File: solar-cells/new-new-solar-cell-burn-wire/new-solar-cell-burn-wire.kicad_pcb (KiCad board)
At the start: 2 copper layers, 80 x 103.5 mm, 22 parts, among them J1 Solar Cell, J2 Burn Wire

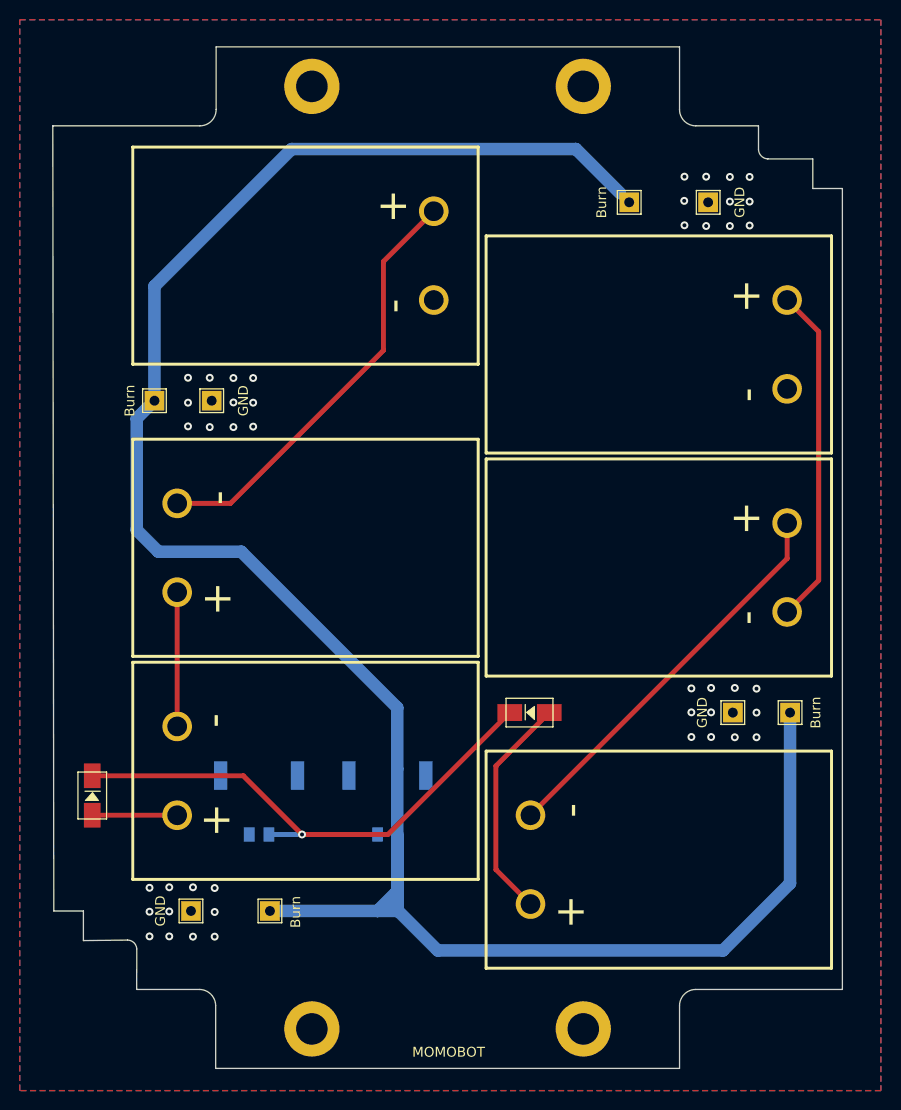
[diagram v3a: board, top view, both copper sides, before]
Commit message: fixed tracks to reduce EMI
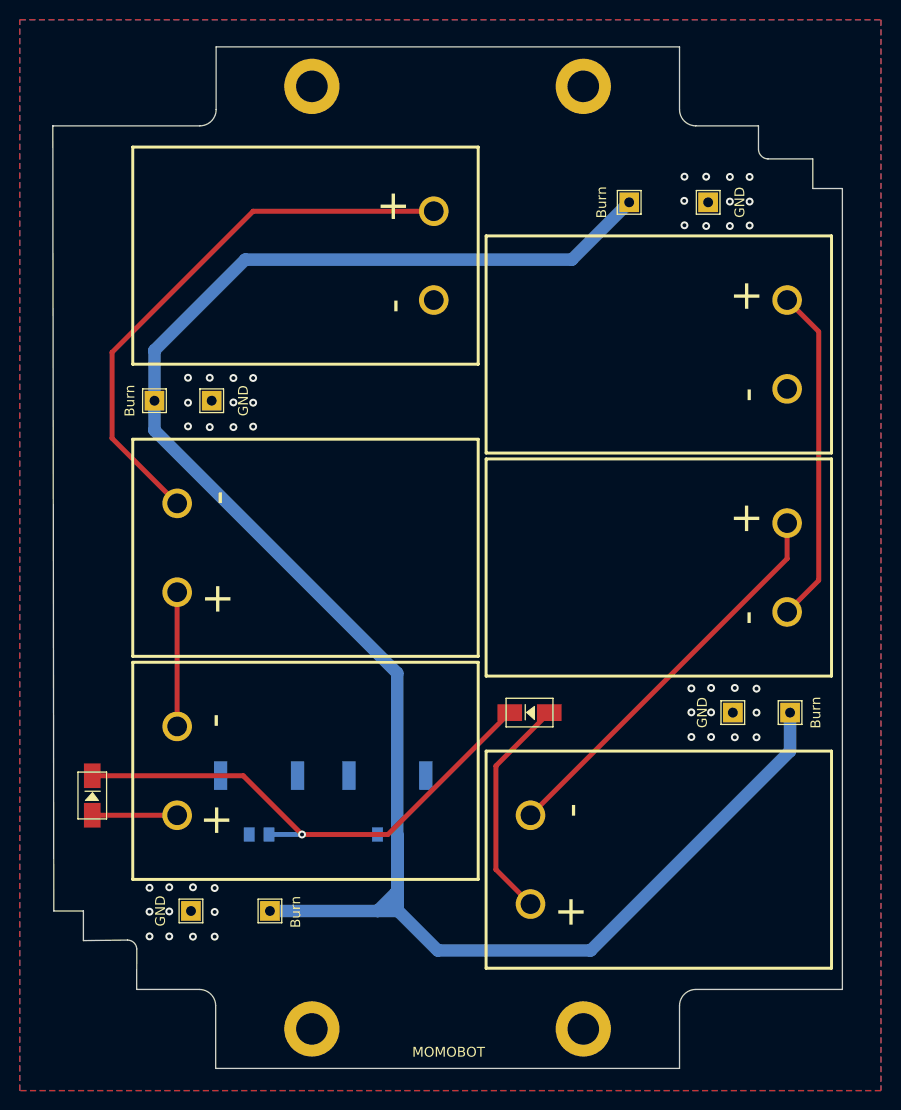
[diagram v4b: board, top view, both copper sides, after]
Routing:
- net BURN: track 220.9 -> 198.4 mm
- net Net-(SC2-Pad2): track 43.5 -> 56.6 mm
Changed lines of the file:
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@@
   (via (at 136.075 54.35) (size 0.8) (drill 0.4) (layers "F.Cu" "B.Cu") (free) (net 1))
   (segment (start 107.000001 118.725) (end 107.000001 126.3) (width 1.27) (layer "B.Cu") (net 2))
-  (segment (start 107.000001 105.700001) (end 107.000001 111.900001) (width 1.27) (layer "B.Cu") (net 2))
-  (segment (start 82.8 89.9) (end 91.2 89.9) (width 1.27) (layer "B.Cu") (net 2))
-  (segment (start 96.3 49.1) (end 82.4 63) (width 1.27) (layer "B.Cu") (net 2))
   (segment (start 105 126.3) (end 94.1 126.3) (width 1.27) (layer "B.Cu") (net 2))
-  (segment (start 82.4 63) (end 82.4 74.6) (width 1.27) (layer "B.Cu") (net 2))
+  (segment (start 111.1 130.3) (end 126.6 130.3) (width 1.27) (layer "B.Cu") (net 2))
   (segment (start 107.000001 118.55) (end 107.000001 124.399999) (width 1.27) (layer "B.Cu") (net 2))
-  (segment (start 80.6 76.4) (end 80.6 87.7) (width 1.27) (layer "B.Cu") (net 2))
+  (segment (start 146.8 110.1) (end 146.8 106.2) (width 1.27) (layer "B.Cu") (net 2))
   (segment (start 107.000001 118.55) (end 107.000001 118.725) (width 0.25) (layer "B.Cu") (net 2))
+  (segment (start 107.000001 126.3) (end 105 126.3) (width 1.27) (layer "B.Cu") (net 2))
   (segment (start 107.000001 126.200001) (end 111.1 130.3) (width 1.27) (layer "B.Cu") (net 2))
-  (segment (start 107.000001 126.3) (end 105 126.3) (width 1.27) (layer "B.Cu") (net 2))
-  (segment (start 146.8 123.5) (end 146.8 106.2) (width 1.27) (layer "B.Cu") (net 2))
-  (segment (start 111.1 130.3) (end 140 130.3) (width 1.27) (layer "B.Cu") (net 2))
-  (segment (start 80.6 87.7) (end 82.8 89.9) (width 1.27) (layer "B.Cu") (net 2))
-  (segment (start 91.2 89.9) (end 107.000001 105.700001) (width 1.27) (layer "B.Cu") (net 2))
-  (segment (start 125.1 49.1) (end 96.3 49.1) (width 1.27) (layer "B.Cu") (net 2))
-  (segment (start 129.575 53.575) (end 125.1 49.1) (width 1.27) (layer "B.Cu") (net 2))
+  (segment (start 130.5 54.5) (end 124.7 60.3) (width 1.27) (layer "B.Cu") (net 2))
+  (segment (start 107.000001 102.200001) (end 107.000001 118.55) (width 1.27) (layer "B.Cu") (net 2))
+  (segment (start 126.6 130.3) (end 146.8 110.1) (width 1.27) (layer "B.Cu") (net 2))
+  (segment (start 82.4 69.5) (end 82.4 74.6) (width 1.27) (layer "B.Cu") (net 2))
   (segment (start 106.900001 124.399999) (end 107.000001 124.399999) (width 1.27) (layer "B.Cu") (net 2))
-  (segment (start 130.5 54.5) (end 129.575 53.575) (width 0.25) (layer "B.Cu") (net 2))
+  (segment (start 82.4 77.6) (end 107.000001 102.200001) (width 1.27) (layer "B.Cu") (net 2))
+  (segment (start 124.7 60.3) (end 91.6 60.3) (width 1.27) (layer "B.Cu") (net 2))
+  (segment (start 107.000001 124.399999) (end 107.000001 126.200001) (width 1.27) (layer "B.Cu") (net 2))
   (segment (start 105 126.3) (end 106.900001 124.399999) (width 1.27) (layer "B.Cu") (net 2))
-  (segment (start 82.4 74.6) (end 80.6 76.4) (width 1.27) (layer "B.Cu") (net 2))
-  (segment (start 107.000001 124.399999) (end 107.000001 126.200001) (width 1.27) (layer "B.Cu") (net 2))
-  (segment (start 140 130.3) (end 146.8 123.5) (width 1.27) (layer "B.Cu") (net 2))
-  (segment (start 107.000001 111.900001) (end 107.000001 118.55) (width 1.27) (layer "B.Cu") (net 2))
+  (segment (start 91.6 60.3) (end 82.4 69.5) (width 1.27) (layer "B.Cu") (net 2))
+  (segment (start 82.4 74.6) (end 82.4 77.6) (width 1.27) (layer "B.Cu") (net 2))
   (segment (start 84.7 94) (end 84.7 107.6) (width 0.5) (layer "F.Cu") (net 3))
   (segment (start 84.7 116.6) (end 76.1 116.6) (width 0.5) (layer "F.Cu") (net 4))
@@
   (segment (start 117 111.6) (end 117 122.1) (width 0.5) (layer "F.Cu") (net 5))
   (segment (start 122.4 106.2) (end 117 111.6) (width 0.5) (layer "F.Cu") (net 5))
-  (segment (start 90.1 85) (end 84.7 85) (width 0.5) (layer "F.Cu") (net 6))
-  (segment (start 105.6 69.5) (end 90.1 85) (width 0.5) (layer "F.Cu") (net 6))
-  (segment (start 105.6 60.5) (end 105.6 69.5) (width 0.5) (layer "F.Cu") (net 6))
-  (segment (start 110.7 55.4) (end 105.6 60.5) (width 0.5) (layer "F.Cu") (net 6))
+  (segment (start 92.4 55.4) (end 110.7 55.4) (width 0.5) (layer "F.Cu") (net 6))
+  (segment (start 78.1 78.4) (end 78.1 69.7) (width 0.5) (layer "F.Cu") (net 6))
+  (segment (start 84.7 85) (end 78.1 78.4) (width 0.5) (layer "F.Cu") (net 6))
+  (segment (start 78.1 69.7) (end 92.4 55.4) (width 0.5) (layer "F.Cu") (net 6))
   (segment (start 146.5 90.6) (end 120.5 116.6) (width 0.5) (layer "F.Cu") (net 7))
   (segment (start 146.5 87) (end 146.5 90.6) (width 0.5) (layer "F.Cu") (net 7))
@@
   (segment (start 149.7 92.8) (end 146.5 96) (width 0.5) (layer "F.Cu") (net 8))
   (segment (start 97.35 118.55) (end 91.4 112.6) (width 0.5) (layer "F.Cu") (net 9))
-  (segment (start 97.25 118.55) (end 97.35 118.55) (width 0.25) (layer "F.Cu") (net 9))
   (segment (start 97.35 118.55) (end 106.05 118.55) (width 0.5) (layer "F.Cu") (net 9))
   (segment (start 106.05 118.55) (end 118.4 106.2) (width 0.5) (layer "F.Cu") (net 9))

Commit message: fixed routing, added vias
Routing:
- net VSOLAR: track 53.2 -> 60.9 mm
- net GND: vias 44 -> 56
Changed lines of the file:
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@@
   )
   (via (at 81.9 128.875) (size 0.8) (drill 0.4) (layers "F.Cu" "B.Cu") (free) (net 1))
-  (via (at 85.8 77.2) (size 0.8) (drill 0.4) (layers "F.Cu" "B.Cu") (free) (net 1))
+  (via (at 114.4 66.1) (size 0.8) (drill 0.4) (layers "F.Cu" "B.Cu") (free) (net 1))
+  (via (at 113.5 64.2) (size 0.8) (drill 0.4) (layers "F.Cu" "B.Cu") (free) (net 1))
   (via (at 136.8 106.175) (size 0.8) (drill 0.4) (layers "F.Cu" "B.Cu") (free) (net 1))
-  (via (at 136.1 51.9) (size 0.8) (drill 0.4) (layers "F.Cu" "B.Cu") (free) (net 1))
   (via (at 81.9 123.95) (size 0.8) (drill 0.4) (layers "F.Cu" "B.Cu") (free) (net 1))
   (via (at 140.7 51.925) (size 0.8) (drill 0.4) (layers "F.Cu" "B.Cu") (free) (net 1))
   (via (at 138.8 106.175) (size 0.8) (drill 0.4) (layers "F.Cu" "B.Cu") (free) (net 1))
-  (via (at 143.4 103.775) (size 0.8) (drill 0.4) (layers "F.Cu" "B.Cu") (free) (net 1))
+  (via (at 145.4 76.8) (size 0.8) (drill 0.4) (layers "F.Cu" "B.Cu") (free) (net 1))
   (via (at 90.4 72.3) (size 0.8) (drill 0.4) (layers "F.Cu" "B.Cu") (free) (net 1))
   (via (at 141.2 108.7) (size 0.8) (drill 0.4) (layers "F.Cu" "B.Cu") (free) (net 1))
   (via (at 90.4 74.775) (size 0.8) (drill 0.4) (layers "F.Cu" "B.Cu") (free) (net 1))
-  (via (at 85.8 72.275) (size 0.8) (drill 0.4) (layers "F.Cu" "B.Cu") (free) (net 1))
+  (via (at 144.2 70) (size 0.8) (drill 0.4) (layers "F.Cu" "B.Cu") (free) (net 1))
+  (via (at 108 66) (size 0.8) (drill 0.4) (layers "F.Cu" "B.Cu") (free) (net 1))
   (via (at 83.9 123.9) (size 0.8) (drill 0.4) (layers "F.Cu" "B.Cu") (free) (net 1))
+  (via (at 144.2 76.3) (size 0.8) (drill 0.4) (layers "F.Cu" "B.Cu") (free) (net 1))
+  (via (at 110.8 67.4) (size 0.8) (drill 0.4) (layers "F.Cu" "B.Cu") (free) (net 1))
+  (via (at 144.2 71.3) (size 0.8) (drill 0.4) (layers "F.Cu" "B.Cu") (free) (net 1))
+  (via (at 143.4 75.2) (size 0.8) (drill 0.4) (layers "F.Cu" "B.Cu") (free) (net 1))
   (via (at 83.9 126.35) (size 0.8) (drill 0.4) (layers "F.Cu" "B.Cu") (free) (net 1))
   (via (at 83.9 128.875) (size 0.8) (drill 0.4) (layers "F.Cu" "B.Cu") (free) (net 1))
   (via (at 92.4 77.225) (size 0.8) (drill 0.4) (layers "F.Cu" "B.Cu") (free) (net 1))
+  (via (at 107.3 67.2) (size 0.8) (drill 0.4) (layers "F.Cu" "B.Cu") (free) (net 1))
   (via (at 142.7 51.925) (size 0.8) (drill 0.4) (layers "F.Cu" "B.Cu") (free) (net 1))
-  (via (at 88.5 123.975) (size 0.8) (drill 0.4) (layers "F.Cu" "B.Cu") (free) (net 1))
+  (via (at 143.9 74.1) (size 0.8) (drill 0.4) (layers "F.Cu" "B.Cu") (free) (net 1))
   (via (at 136.8 108.675) (size 0.8) (drill 0.4) (layers "F.Cu" "B.Cu") (free) (net 1))
-  (via (at 88.5 128.9) (size 0.8) (drill 0.4) (layers "F.Cu" "B.Cu") (free) (net 1))
+  (via (at 144.7 75.4) (size 0.8) (drill 0.4) (layers "F.Cu" "B.Cu") (free) (net 1))
+  (via (at 108.7 68.5) (size 0.8) (drill 0.4) (layers "F.Cu" "B.Cu") (free) (net 1))
   (via (at 88 77.275) (size 0.8) (drill 0.4) (layers "F.Cu" "B.Cu") (free) (net 1))
+  (via (at 107.7 64.4) (size 0.8) (drill 0.4) (layers "F.Cu" "B.Cu") (free) (net 1))
+  (via (at 113.4 67.7) (size 0.8) (drill 0.4) (layers "F.Cu" "B.Cu") (free) (net 1))
   (via (at 92.4 72.3) (size 0.8) (drill 0.4) (layers "F.Cu" "B.Cu") (free) (net 1))
   (via (at 142.7 56.85) (size 0.8) (drill 0.4) (layers "F.Cu" "B.Cu") (free) (net 1))
-  (via (at 143.4 108.7) (size 0.8) (drill 0.4) (layers "F.Cu" "B.Cu") (free) (net 1))
+  (via (at 109.1 67.2) (size 0.8) (drill 0.4) (layers "F.Cu" "B.Cu") (free) (net 1))
   (via (at 138.8 108.675) (size 0.8) (drill 0.4) (layers "F.Cu" "B.Cu") (free) (net 1))
   (via (at 92.4 74.8) (size 0.8) (drill 0.4) (layers "F.Cu" "B.Cu") (free) (net 1))
-  (via (at 143.4 106.2) (size 0.8) (drill 0.4) (layers "F.Cu" "B.Cu") (free) (net 1))
+  (via (at 143.9 72.5) (size 0.8) (drill 0.4) (layers "F.Cu" "B.Cu") (free) (net 1))
   (via (at 138.3 56.9) (size 0.8) (drill 0.4) (layers "F.Cu" "B.Cu") (free) (net 1))
+  (via (at 143.1 70.9) (size 0.8) (drill 0.4) (layers "F.Cu" "B.Cu") (free) (net 1))
   (via (at 90.4 77.275) (size 0.8) (drill 0.4) (layers "F.Cu" "B.Cu") (free) (net 1))
-  (via (at 85.8 74.8) (size 0.8) (drill 0.4) (layers "F.Cu" "B.Cu") (free) (net 1))
+  (via (at 113.3 65.6) (size 0.8) (drill 0.4) (layers "F.Cu" "B.Cu") (free) (net 1))
   (via (at 138.3 51.9) (size 0.8) (drill 0.4) (layers "F.Cu" "B.Cu") (free) (net 1))
   (via (at 140.7 56.9) (size 0.8) (drill 0.4) (layers "F.Cu" "B.Cu") (free) (net 1))
-  (via (at 136.8 103.75) (size 0.8) (drill 0.4) (layers "F.Cu" "B.Cu") (free) (net 1))
+  (via (at 145.3 70.7) (size 0.8) (drill 0.4) (layers "F.Cu" "B.Cu") (free) (net 1))
+  (via (at 142.8 72) (size 0.8) (drill 0.4) (layers "F.Cu" "B.Cu") (free) (net 1))
   (via (at 138.8 103.7) (size 0.8) (drill 0.4) (layers "F.Cu" "B.Cu") (free) (net 1))
   (via (at 81.9 126.375) (size 0.8) (drill 0.4) (layers "F.Cu" "B.Cu") (free) (net 1))
@@
   (via (at 88 72.275) (size 0.8) (drill 0.4) (layers "F.Cu" "B.Cu") (free) (net 1))
   (via (at 140.7 54.425) (size 0.8) (drill 0.4) (layers "F.Cu" "B.Cu") (free) (net 1))
-  (via (at 136.1 56.825) (size 0.8) (drill 0.4) (layers "F.Cu" "B.Cu") (free) (net 1))
-  (via (at 88.5 126.4) (size 0.8) (drill 0.4) (layers "F.Cu" "B.Cu") (free) (net 1))
-  (via (at 136.075 54.35) (size 0.8) (drill 0.4) (layers "F.Cu" "B.Cu") (free) (net 1))
+  (via (at 110.5 68.8) (size 0.8) (drill 0.4) (layers "F.Cu" "B.Cu") (free) (net 1))
+  (via (at 112 68.5) (size 0.8) (drill 0.4) (layers "F.Cu" "B.Cu") (free) (net 1))
+  (via (at 112.4 66.8) (size 0.8) (drill 0.4) (layers "F.Cu" "B.Cu") (free) (net 1))
+  (via (at 146.1 75.9) (size 0.8) (drill 0.4) (layers "F.Cu" "B.Cu") (free) (net 1))
   (segment (start 107.000001 118.725) (end 107.000001 126.3) (width 1.27) (layer "B.Cu") (net 2))
   (segment (start 105 126.3) (end 94.1 126.3) (width 1.27) (layer "B.Cu") (net 2))
@@
   (segment (start 146.8 110.1) (end 146.8 106.2) (width 1.27) (layer "B.Cu") (net 2))
   (segment (start 107.000001 118.55) (end 107.000001 118.725) (width 0.25) (layer "B.Cu") (net 2))
+  (segment (start 125.4 59.6) (end 92.3 59.6) (width 1.27) (layer "B.Cu") (net 2))
   (segment (start 107.000001 126.3) (end 105 126.3) (width 1.27) (layer "B.Cu") (net 2))
   (segment (start 107.000001 126.200001) (end 111.1 130.3) (width 1.27) (layer "B.Cu") (net 2))
-  (segment (start 130.5 54.5) (end 124.7 60.3) (width 1.27) (layer "B.Cu") (net 2))
   (segment (start 107.000001 102.200001) (end 107.000001 118.55) (width 1.27) (layer "B.Cu") (net 2))
   (segment (start 126.6 130.3) (end 146.8 110.1) (width 1.27) (layer "B.Cu") (net 2))
+  (segment (start 106.900001 124.399999) (end 107.000001 124.399999) (width 1.27) (layer "B.Cu") (net 2))
+  (segment (start 130.5 54.5) (end 125.4 59.6) (width 1.27) (layer "B.Cu") (net 2))
+  (segment (start 82.4 77.6) (end 107.000001 102.200001) (width 1.27) (layer "B.Cu") (net 2))
+  (segment (start 107.000001 124.399999) (end 107.000001 126.200001) (width 1.27) (layer "B.Cu") (net 2))
   (segment (start 82.4 69.5) (end 82.4 74.6) (width 1.27) (layer "B.Cu") (net 2))
-  (segment (start 106.900001 124.399999) (end 107.000001 124.399999) (width 1.27) (layer "B.Cu") (net 2))
-  (segment (start 82.4 77.6) (end 107.000001 102.200001) (width 1.27) (layer "B.Cu") (net 2))
-  (segment (start 124.7 60.3) (end 91.6 60.3) (width 1.27) (layer "B.Cu") (net 2))
-  (segment (start 107.000001 124.399999) (end 107.000001 126.200001) (width 1.27) (layer "B.Cu") (net 2))
+  (segment (start 92.3 59.6) (end 82.4 69.5) (width 1.27) (layer "B.Cu") (net 2))
   (segment (start 105 126.3) (end 106.900001 124.399999) (width 1.27) (layer "B.Cu") (net 2))
-  (segment (start 91.6 60.3) (end 82.4 69.5) (width 1.27) (layer "B.Cu") (net 2))
   (segment (start 82.4 74.6) (end 82.4 77.6) (width 1.27) (layer "B.Cu") (net 2))
   (segment (start 84.7 94) (end 84.7 107.6) (width 0.5) (layer "F.Cu") (net 3))
@@
   (segment (start 149.7 67.6) (end 149.7 92.8) (width 0.5) (layer "F.Cu") (net 8))
   (segment (start 149.7 92.8) (end 146.5 96) (width 0.5) (layer "F.Cu") (net 8))
+  (segment (start 111.5 121.7) (end 114.2 119) (width 0.5) (layer "F.Cu") (net 9))
+  (segment (start 100.5 121.7) (end 111.5 121.7) (width 0.5) (layer "F.Cu") (net 9))
+  (segment (start 97.35 118.55) (end 100.5 121.7) (width 0.5) (layer "F.Cu") (net 9))
   (segment (start 97.35 118.55) (end 91.4 112.6) (width 0.5) (layer "F.Cu") (net 9))
-  (segment (start 97.35 118.55) (end 106.05 118.55) (width 0.5) (layer "F.Cu") (net 9))
-  (segment (start 106.05 118.55) (end 118.4 106.2) (width 0.5) (layer "F.Cu") (net 9))
+  (segment (start 114.2 110.4) (end 118.4 106.2) (width 0.5) (layer "F.Cu") (net 9))
   (segment (start 91.4 112.6) (end 76.1 112.6) (width 0.5) (layer "F.Cu") (net 9))
+  (segment (start 114.2 119) (end 114.2 110.4) (width 0.5) (layer "F.Cu") (net 9))
   (via (at 97.35 118.55) (size 0.8) (drill 0.4) (layers "F.Cu" "B.Cu") (net 9))
   (segment (start 94.000001 118.55) (end 97.35 118.55) (width 0.5) (layer "B.Cu") (net 9))
